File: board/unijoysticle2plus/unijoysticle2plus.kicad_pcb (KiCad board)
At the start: 4 copper layers, 62 x 49 mm, 44 parts, among them J1 DB9_Female, J2 DB9_Female, J3 USB_B_Micro, Q1 S8050, Q2 S8050, SW1 RESET, SW2 JOY SWAP, SW3 BOOT, U1 74HC05, U2 74HC05, U3 74HC05, U4 ESP32-WROOM-32E, U5 AMS1117-3.3, U6 CH340C

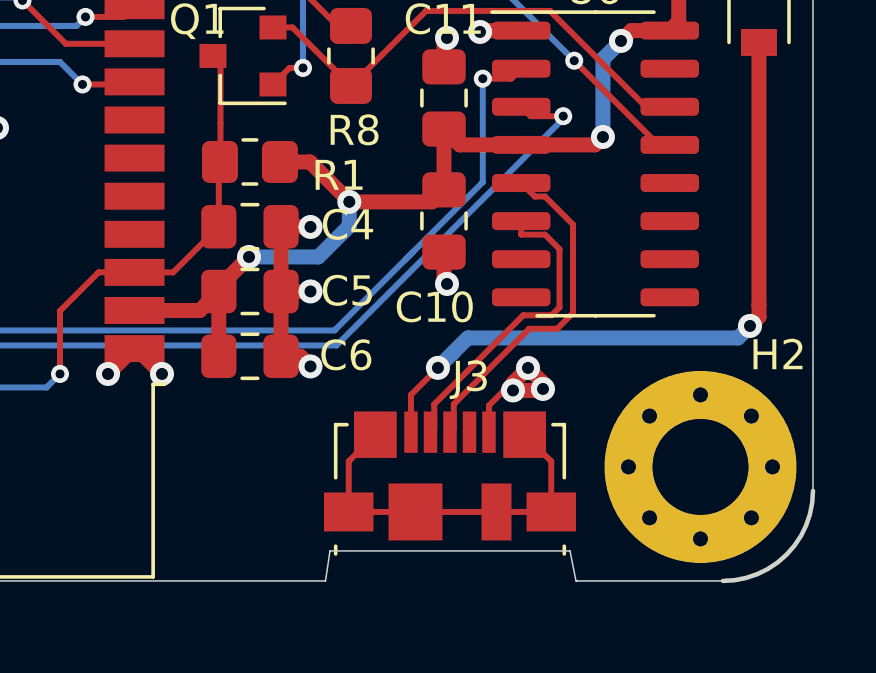
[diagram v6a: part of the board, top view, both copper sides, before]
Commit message: unijoysticle 2+: use better USB micro B connector
The one used in Rev F works Ok when the Fab house solder it correctly.
But it might be possible that it might not work. At least I found 1 / 20
that was not working due to a bad solder/alignment (?) in one of the
boards.

So, I'm switching to one that has some holes so the alignment should not
fail. It might required some extra manual solder... but we shall see.

Also, I slightly improved the routing traces between the USB D- / D+
with the CH340 chip.

Also, I'm using 1.5K resitor for Green LED as well.
The previous LED that was used in Rev F is no longer available and the
2nd batch came with a more potent one. So I need to increase the
resistor.

Besides those two little changes, everything is the same.
Revistion G and F are functionality-wise the same.
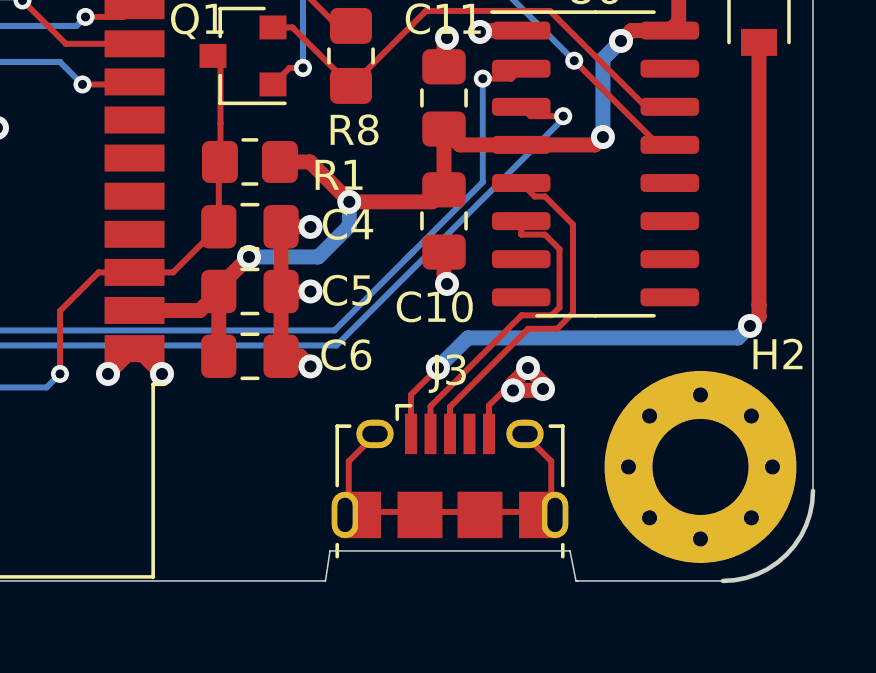
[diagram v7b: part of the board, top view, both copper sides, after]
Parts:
- J3: footprint Connector_USB:USB_Micro-B_Molex_47346-0001 -> Connector_USB:USB_Micro-B_Amphenol_10118194_Horizontal
- R3: value 330 -> 1.5k
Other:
- board text added: "Unijoysticle 2+ Rev. G"
- board text removed: "Unijoysticle 2+ Rev. F"

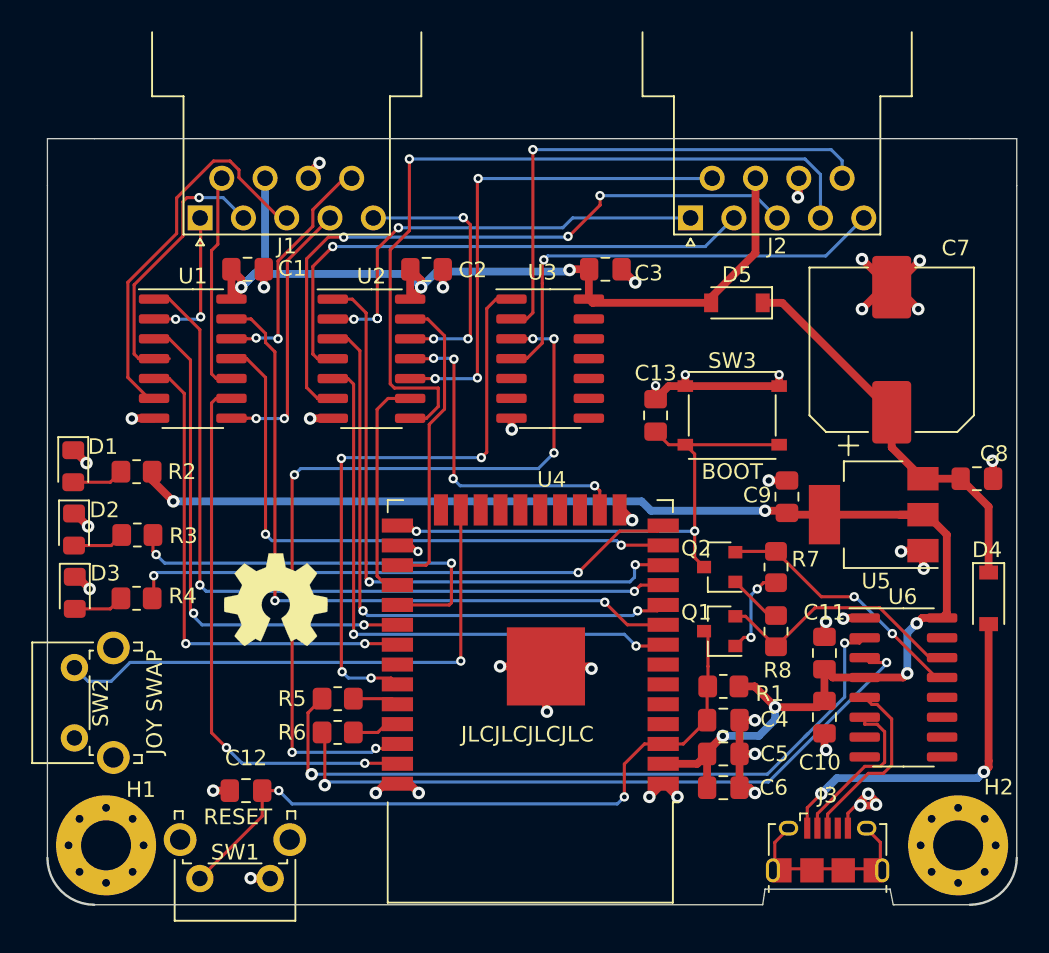
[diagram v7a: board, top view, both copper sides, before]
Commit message: unijoysticle2+: kicad 6 migration
Migrates Unijoysticle 2+ Kicad 5 files to Kicad 6

In the process, it bumps version to Rev. H.
The schematic is the "same": just minor cosmetic changes were done only
to make ERC happy.

Similar on the PCB: it is the same, but NET-R5-PAD2 and NET-R6-PAD2 were
re-routed again since "Tools -> Clean up vias and tracks" removed it.

Besides that, the shcematic and layout are the same...
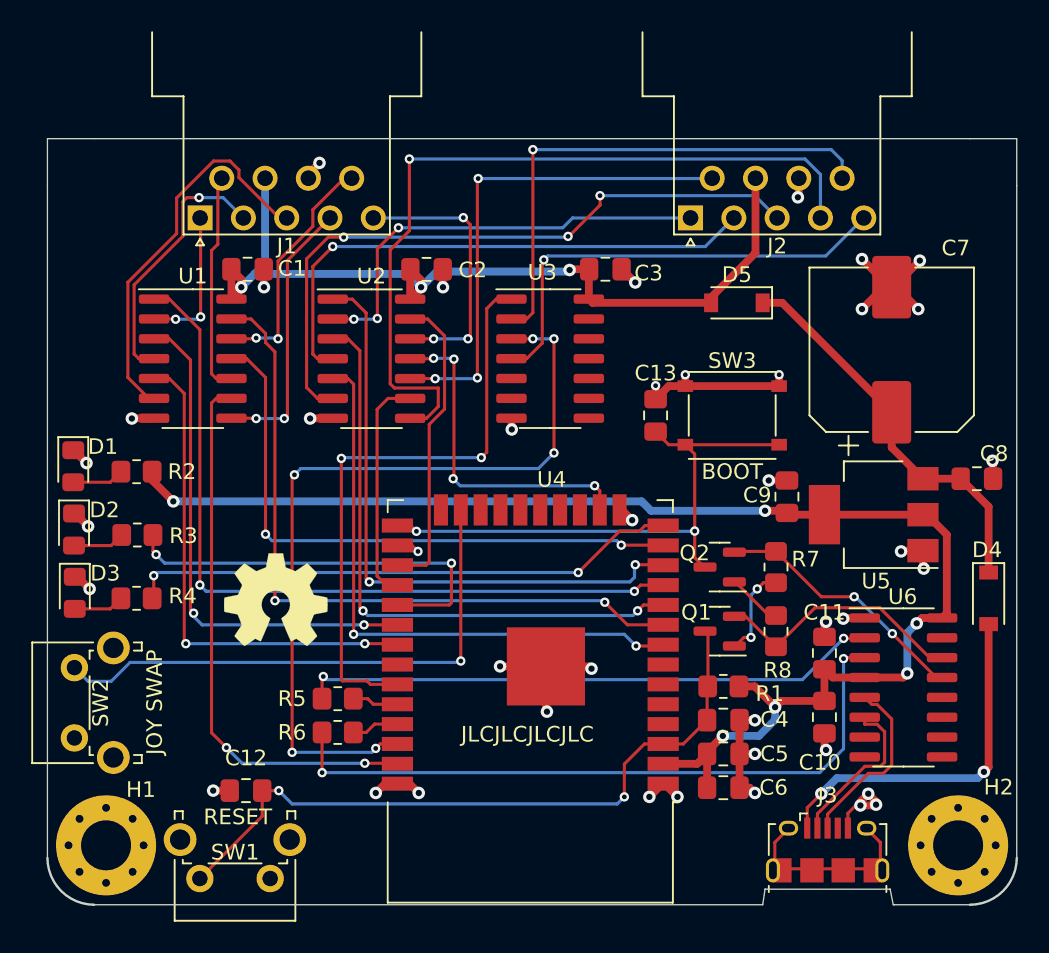
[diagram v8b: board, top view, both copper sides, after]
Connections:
- J3 pad 4: (no net) -> unconnected-(J3-Pad4)
- J3 pad 6: Net-(J3-Pad6) -> unconnected-(J3-Pad6)
- U4 pad 17: (no net) -> unconnected-(U4-Pad17)
- U4 pad 18: (no net) -> unconnected-(U4-Pad18)
- U4 pad 19: (no net) -> unconnected-(U4-Pad19)
- U4 pad 20: (no net) -> unconnected-(U4-Pad20)
- U4 pad 21: (no net) -> unconnected-(U4-Pad21)
- U4 pad 22: (no net) -> unconnected-(U4-Pad22)
- U4 pad 24: (no net) -> unconnected-(U4-Pad24)
- U4 pad 32: (no net) -> unconnected-(U4-Pad32)
- U4 pad 4: (no net) -> /GPIO36
- U4 pad 5: (no net) -> /GPIO39
- U4 pad 6: (no net) -> /GPIO34
- U4 pad 7: (no net) -> /GPIO35
- U6 pad 10: (no net) -> unconnected-(U6-Pad10)
- U6 pad 11: (no net) -> unconnected-(U6-Pad11)
- U6 pad 12: (no net) -> unconnected-(U6-Pad12)
- U6 pad 15: (no net) -> unconnected-(U6-Pad15)
- U6 pad 7: (no net) -> unconnected-(U6-Pad7)
- U6 pad 8: (no net) -> unconnected-(U6-Pad8)
- U6 pad 9: (no net) -> unconnected-(U6-Pad9)
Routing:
- net unconnected-(J3-Pad6): track 0.00 -> 12.6 mm
- net Net-(J3-Pad6): track 12.6 -> 0.00 mm
- net Net-(R5-Pad2): track 47.4 -> 37.3 mm
- net GND: track 74.9 -> 72.2 mm, vias 42 -> 41
- net +3V3: track 91.1 -> 88.7 mm
- net /GPIO_J1_UP: track 51.8 -> 50.0 mm
- net +5V: track 59.2 -> 57.5 mm
- net /J1_POTX: track 16.5 -> 15.5 mm
- net /J1_RIGHT: track 18.4 -> 17.4 mm
- net /J1_DOWN: track 17.9 -> 16.9 mm
- net /J2_FIRE: track 33.0 -> 32.1 mm
- net /GPIO_J2_POTY: track 52.9 -> 52.0 mm
- net Net-(R6-Pad2): track 44.2 -> 43.7 mm
- net /GPIO_J2_POTX: track 38.0 -> 38.4 mm, vias 4 -> 2
- net /J2_UP: vias 4 -> 3
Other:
- net class Default removed
- net class GND removed
- net class POWER removed
- board text added: "Unijoysticle 2+ Rev. H"
- board text removed: "Unijoysticle 2+ Rev. G"
